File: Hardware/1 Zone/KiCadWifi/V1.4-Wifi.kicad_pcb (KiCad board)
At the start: 2 copper layers, 100 x 80 mm, 133 parts, among them CN11 Pinheader 1x12 P2.54 Horizont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, CN16 Pinheader 1x02 P2.54 Horizont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, J1 Screw_Terminal_01x02, Q1 IPD90N04S403ATMA1, Q10 PJA3404A, Q11 PJA3404A, Q12 BC816-16VL, Q8 UMH3NTN, SW1 K2-1102DP-G3SW-04, SW2 K2-1102DP-G3SW-04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

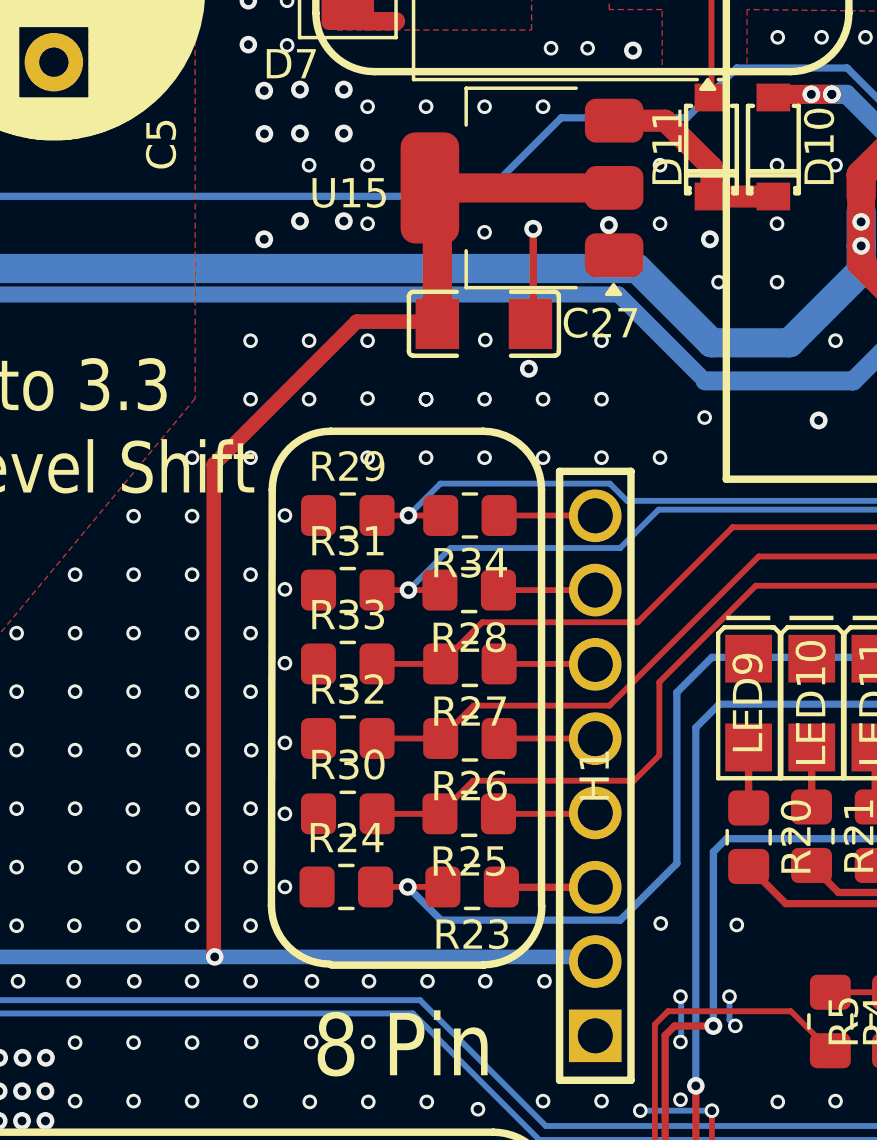
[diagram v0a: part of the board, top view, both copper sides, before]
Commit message: Changed C27 to T491B107M010AT due to availablility
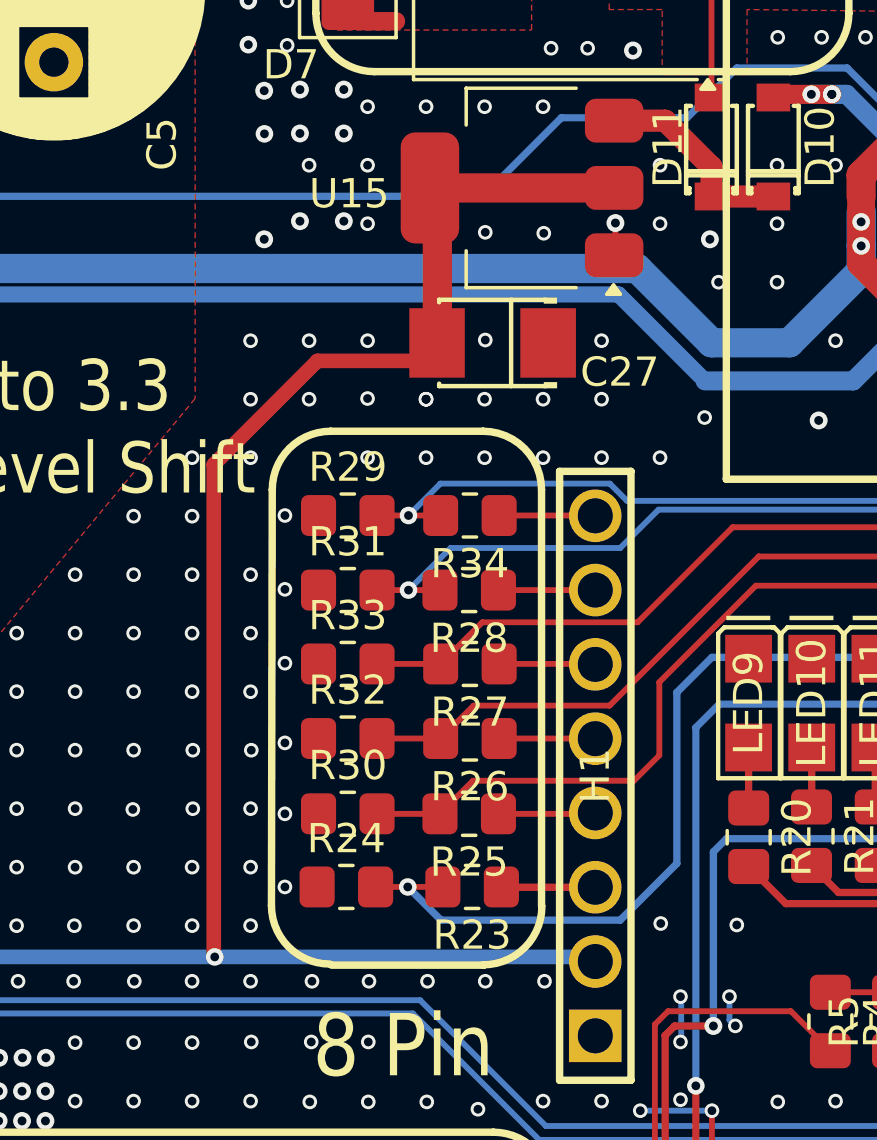
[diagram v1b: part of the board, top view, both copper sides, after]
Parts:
- C27: footprint V1.4-Wifi-easyedapro:C1206 -> V1.4-Wifi-easyedapro:CAP-SMD_L3.5-W2.8-R-RD
- moved C27 0.72 mm to (155.0, 98.2)
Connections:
- C27 pad 1: 3.3V -> GND
- C27 pad 2: GND -> 3.3V
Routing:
- net GND: track 66.4 -> 63.6 mm, vias 698 -> 697
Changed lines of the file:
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@@
 		)
 	)
-	(footprint "V1.4-Wifi-easyedapro:C1206"
+	(footprint "V1.4-Wifi-easyedapro:CAP-SMD_L3.5-W2.8-R-RD"
 		(layer "F.Cu")
-		(at 154.7035 97.5455)
+		(at 155 98.2)
 		(property "Reference" "C27"
-			(at 4.0035 0 0)
+			(at 4.35 1 0)
 			(layer "F.SilkS")
 			(effects
@@
 			)
 		)
-		(property "Datasheet" "https://atta.szlcsc.com/upload/public/pdf/source/20160103/1457707673200.pdf"
+		(property "Datasheet" "https://eu.mouser.com/datasheet/2/447/KEM_T2005_T491-3316937.pdf"
 			(at 0 0 0)
 			(layer "F.Fab")
@@
 			)
 		)
-		(property "Manufacturer" "SAMSUNG"
+		(property "Manufacturer" "KEMET"
 			(at 0 0 0)
 			(unlocked yes)
@@
 			)
 		)
-		(property "mpn" "CL31A107MQHNNNE"
+		(property "mpn" "T491B107M010AT"
 			(at 0 0 0)
 			(unlocked yes)
@@
 		(sheetfile "V1.4-Wifi.kicad_sch")
 		(fp_line
-			(start -2.5635 0.94)
-			(end -2.5635 -0.94)
+			(start -1.826 -1.476)
+			(end -1.826 -1.391)
 			(stroke
 				(width 0.1525)
@@
 		)
 		(fp_line
-			(start -2.411 -1.0925)
-			(end -0.926 -1.0925)
+			(start -1.826 -1.476)
+			(end 1.826 -1.476)
 			(stroke
 				(width 0.1525)
@@
 		)
 		(fp_line
-			(start -0.926 1.0925)
-			(end -2.411 1.0925)
+			(start -1.826 1.476)
+			(end -1.826 1.391)
 			(stroke
 				(width 0.1525)
@@
 		)
 		(fp_line
-			(start 0.926 1.0925)
-			(end 2.411 1.0925)
+			(start -1.826 1.476)
+			(end 1.826 1.476)
 			(stroke
 				(width 0.1525)
@@
 		)
 		(fp_line
-			(start 2.411 -1.0925)
-			(end 0.926 -1.0925)
+			(start 0.635 -1.476)
+			(end 0.635 1.476)
 			(stroke
 				(width 0.1525)
@@
 			(layer "F.SilkS")
 		)
-		(fp_line
-			(start 2.5635 0.94)
-			(end 2.5635 -0.94)
+		(fp_poly
+			(pts
+				(xy 1.75 -1.5525) (xy 1.75 -1.3405) (xy 2.207 -1.3405) (xy 2.207 -1.5525)
+			)
 			(stroke
-				(width 0.1525)
+				(width 0)
 				(type default)
 			)
+			(fill yes)
 			(layer "F.SilkS")
 		)
-		(fp_arc
-			(start -2.5635 -0.94)
-			(mid -2.518834 -1.047834)
-			(end -2.411 -1.0925)
+		(fp_poly
+			(pts
+				(xy 1.75 1.5525) (xy 1.75 1.3405) (xy 2.207 1.3405) (xy 2.207 1.5525)
+			)
 			(stroke
-				(width 0.1525)
+				(width 0)
 				(type default)
 			)
+			(fill yes)
 			(layer "F.SilkS")
 		)
-		(fp_arc
-			(start -2.411 1.0925)
-			(mid -2.518834 1.047834)
-			(end -2.5635 0.94)
+		(fp_poly
+			(pts
+				(xy -1.54 0.105) (xy -1.54 -0.105) (xy -0.7 -0.105) (xy -0.7 0.105)
+			)
 			(stroke
-				(width 0.1525)
+				(width 0)
 				(type default)
 			)
-			(layer "F.SilkS")
+			(fill yes)
+			(layer "Dwgs.User")
 		)
-		(fp_arc
-			(start 2.411 -1.0925)
-			(mid 2.518834 -1.047834)
-			(end 2.5635 -0.94)
+		(fp_poly
+			(pts
+				(xy 1.225 0.7) (xy 1.225 -0.7) (xy 1.015 -0.7) (xy 1.015 0.7)
+			)
 			(stroke
-				(width 0.1525)
+				(width 0)
 				(type default)
 			)
-			(layer "F.SilkS")
+			(fill yes)
+			(layer "Dwgs.User")
 		)
-		(fp_arc
-			(start 2.5635 0.94)
-			(mid 2.518834 1.047834)
-			(end 2.411 1.0925)
+		(fp_poly
+			(pts
+				(xy 1.54 0.105) (xy 1.54 -0.105) (xy 0.7 -0.105) (xy 0.7 0.105)
+			)
 			(stroke
-				(width 0.1525)
+				(width 0)
 				(type default)
 			)
-			(layer "F.SilkS")
+			(fill yes)
+			(layer "Dwgs.User")
 		)
 		(fp_poly
 			(pts
-				(xy -0.85 0.764) (xy -0.85 0.394) (xy -0.95 0.294) (xy -1.255 0.294) (xy -1.355 0.194) (xy -1.355 -0.194)
-				(xy -1.255 -0.294) (xy -0.95 -0.294) (xy -0.85 -0.394) (xy -0.85 -0.764) (xy -0.95 -0.864) (xy -2.235 -0.864)
-				(xy -2.335 -0.764) (xy -2.335 0.764) (xy -2.235 0.864) (xy -0.95 0.864)
+				(xy 1.75 -1.4) (xy 1.75 -0.7) (xy 1.33 -0.7) (xy 1.33 -1.4)
 			)
 			(stroke
@@
 			)
 			(fill yes)
-			(layer "F.Paste")
+			(layer "Dwgs.User")
 		)
 		(fp_poly
 			(pts
-				(xy 0.85 0.764) (xy 0.85 0.394) (xy 0.95 0.294) (xy 1.255 0.294) (xy 1.355 0.194) (xy 1.355 -0.194)
-				(xy 1.255 -0.294) (xy 0.95 -0.294) (xy 0.85 -0.394) (xy 0.85 -0.764) (xy 0.95 -0.864) (xy 2.235 -0.864)
-				(xy 2.335 -0.764) (xy 2.335 0.764) (xy 2.235 0.864) (xy 0.95 0.864)
+				(xy 1.75 1.4) (xy 1.75 0.7) (xy 1.33 0.7) (xy 1.33 1.4)
 			)
 			(stroke
@@
 			)
 			(fill yes)
-			(layer "F.Paste")
+			(layer "Dwgs.User")
 		)
 		(fp_poly
 			(pts
-				(xy -1.6 0.8) (xy -1.6 -0.8) (xy -1.1 -0.8) (xy -1.1 0.8)
+				(xy -1.75 1.1) (xy -1.75 -1.1) (xy -1.05 -1.1) (xy -1.05 1.1)
 			)
 			(stroke
@@
 		(fp_poly
 			(pts
-				(xy 1.6 0.8) (xy 1.6 -0.8) (xy 1.1 -0.8) (xy 1.1 0.8)
+				(xy 1.75 1.1) (xy 1.75 -1.1) (xy 1.05 -1.1) (xy 1.05 1.1)
 			)
 			(stroke
@@
 		)
 		(fp_line
-			(start -1.6 -0.8)
-			(end 1.6 -0.8)
+			(start -1.75 -1.4)
+			(end 1.75 -1.4)
 			(stroke
 				(width 0.051)
@@
 		)
 		(fp_line
-			(start -1.6 0.8)
-			(end -1.6 -0.8)
+			(start -1.75 1.4)
+			(end -1.75 -1.4)
 			(stroke
 				(width 0.051)
@@
 		)
 		(fp_line
-			(start 1.6 -0.8)
-			(end 1.6 0.8)
+			(start 1.75 -1.4)
+			(end 1.75 1.4)
 			(stroke
 				(width 0.051)
@@
 		)
 		(fp_line
-			(start 1.6 0.8)
-			(end -1.6 0.8)
+			(start 1.75 1.4)
+			(end -1.75 1.4)
 			(stroke
 				(width 0.051)
@@
 		(fp_poly
 			(pts
-				(xy -1.544567 0.777039) (xy -1.577039 0.744567) (xy -1.622961 0.744567) (xy -1.655433 0.777039)
-				(xy -1.655433 0.822961) (xy -1.622961 0.855433) (xy -1.577039 0.855433) (xy -1.544567 0.822961)
+				(xy 1.805433 -1.422961) (xy 1.772961 -1.455433) (xy 1.727039 -1.455433) (xy 1.694567 -1.422961)
+				(xy 1.694567 -1.377039) (xy 1.727039 -1.344567) (xy 1.772961 -1.344567) (xy 1.805433 -1.377039)
 			)
 			(stroke
@@
 		)
 		(pad "1" smd rect
-			(at -1.5925 0)
-			(size 1.485 1.728)
+			(at 1.8985 0)
+			(size 1.9 2.376)
 			(layers "F.Cu" "F.Mask" "F.Paste")
-			(net 36 "3.3V")
+			(net 1 "GND")
 			(pinfunction "1")
 			(pintype "input")
 		)
 		(pad "2" smd rect
-			(at 1.5925 0)
-			(size 1.485 1.728)
+			(at -1.8985 0)
+			(size 1.9 2.376)
 			(layers "F.Cu" "F.Mask" "F.Paste")
-			(net 1 "GND")
+			(net 36 "3.3V")
 			(pinfunction "2")
 			(pintype "input")
 		)
 		(embedded_fonts no)
-		(model "${KIPRJMOD}/EASYEDA_MODELS/C1206_L3.2-W1.6-H1.3.step"
+		(model "${KIPRJMOD}/EASYEDA_MODELS/CASE-B_L3.5-W2.8-H1.9.step"
 			(offset
 				(xyz 0 0 0)
@@
 			)
 			(rotate
-				(xyz -0 -0 -0)
+				(xyz -0 -0 -180)
 			)
 		)
@@
 	)
 	(segment
+		(start 159.2 95.157)
+		(end 159.157 95.2)
+		(width 0.2)
+		(layer "F.Cu")
+		(net 1)
+	)
+	(segment
 		(start 192.6775 74.0775)
 		(end 190.7 74.0775)
@@
 	)
 	(segment
-		(start 156.388 94.297)
-		(end 156.388 97.454)
-		(width 0.254)
-		(layer "F.Cu")
-		(net 1)
-	)
-	(segment
 		(start 172.4 108.75)
 		(end 171.645 108.75)
@@
 	)
 	(segment
-		(start 158.977 94.906)
-		(end 158.977 94.17)
-		(width 0.254)
-		(layer "F.Cu")
-		(net 1)
-	)
-	(segment
 		(start 190.65 85.7)
 		(end 190.0965 86.2535)
@@
 	)
 	(segment
+		(start 159.2 94.1)
+		(end 159.2 95.157)
+		(width 0.2)
+		(layer "F.Cu")
+		(net 1)
+	)
+	(segment
 		(start 196.9 78.95)
 		(end 196.55 78.6)
@@
 	)
 	(via
-		(at 156.388 94.297)
-		(size 0.61)
-		(drill 0.305)
-		(layers "F.Cu" "B.Cu")
-		(net 1)
-	)
-	(via
 		(at 192.911 84.496)
 		(size 0.61)
@@
 	)
 	(via
-		(at 158.977 94.17)
+		(at 159.2 94.1)
 		(size 0.61)
 		(drill 0.305)
@@
 	)
 	(via
-		(at 154.726 94.417)
+		(at 154.75 94.417)
 		(size 0.5)
 		(drill 0.3)
@@
 	)
 	(via
+		(at 156.75 94.45)
+		(size 0.5)
+		(drill 0.3)
+		(layers "F.Cu" "B.Cu")
+		(net 1)
+	)
+	(via
 		(at 174.726 94.123)
 		(size 0.5)
@@
 	)
 	(via
-		(at 156.2405 99.083)
-		(size 0.61)
-		(drill 0.304)
-		(layers "F.Cu" "B.Cu")
-		(net 1)
-	)
-	(via
 		(at 174.726 78.123)
 		(size 0.5)
@@
 	(segment
 		(start 145.466 102.359)
-		(end 150.353 97.472)
+		(end 149.0125 98.8125)
 		(width 0.5)
 		(layer "F.Cu")
@@
 	)
 	(segment
-		(start 106.05 119)
-		(end 106.05 119.7)
+		(start 152.489 98.8125)
+		(end 153.1015 98.2)
 		(width 0.5)
 		(layer "F.Cu")
@@
 	)
 	(segment
-		(start 106.05 128.9)
-		(end 106.05 129.6)
+		(start 106.05 119)
+		(end 106.05 119.7)
 		(width 0.5)
 		(layer "F.Cu")
@@
 	)
 	(segment
-		(start 150.353 97.472)
-		(end 153.0375 97.472)
+		(start 106.05 128.9)
+		(end 106.05 129.6)
 		(width 0.5)
 		(layer "F.Cu")
@@
 	)
 	(segment
-		(start 153.111 97.5455)
-		(end 153.111 92.974)
+		(start 153.1015 98.2)
+		(end 153.111 98.1905)
 		(width 1)
 		(layer "F.Cu")
@@
 	)
 	(segment
-		(start 145.466 119.1585)
-		(end 145.5 119.1925)
+		(start 149.0125 98.8125)
+		(end 152.489 98.8125)
 		(width 0.5)
 		(layer "F.Cu")
@@
 	)
 	(segment
-		(start 145.466 102.359)
-		(end 145.466 119.1585)
+		(start 145.466 119.1585)
+		(end 145.466 102.359)
 		(width 0.5)
 		(layer "F.Cu")
@@
 	)
 	(segment
+		(start 145.5 119.1925)
+		(end 145.466 119.1585)
+		(width 0.5)
+		(layer "F.Cu")
+		(net 36)
+	)
+	(segment
 		(start 106.05 122.5)
 		(end 106.05 128.9)
@@
 		(layer "F.Cu")
 		(net 36)
+	)
+	(segment
+		(start 153.111 98.1905)
+		(end 153.111 92.974)
+		(width 1)
+		(layer "F.Cu")
+		(net 36)

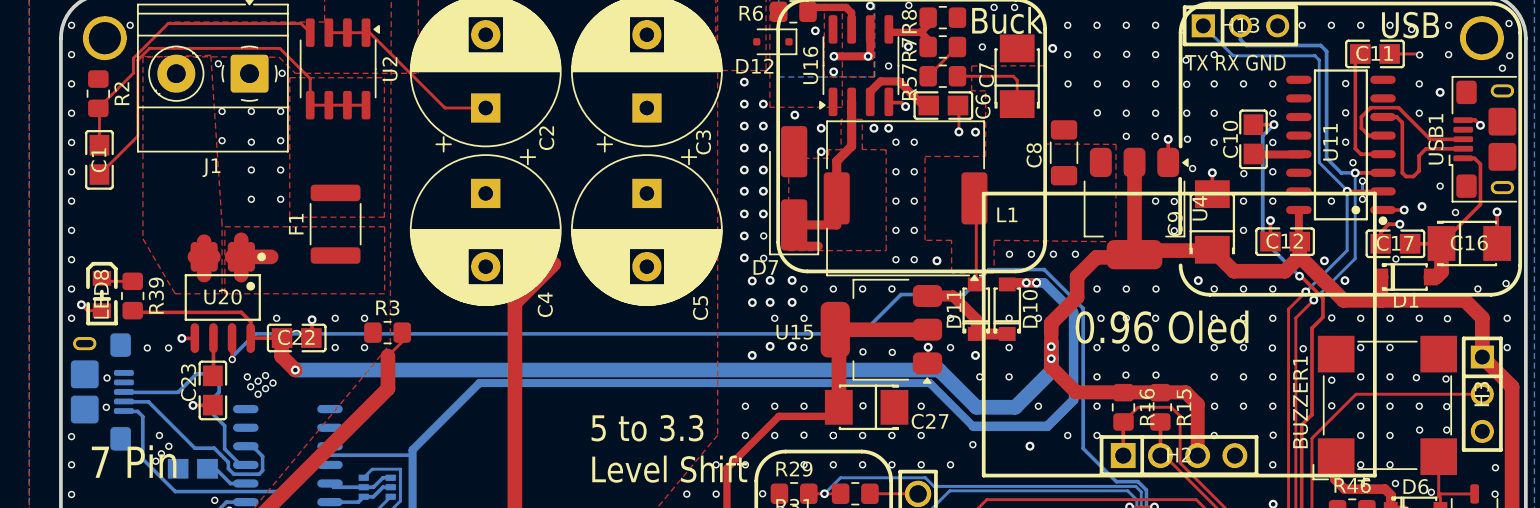
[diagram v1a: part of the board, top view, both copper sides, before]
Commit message: Moved C27 to avoid disrupting D+_E, D-_E return paths
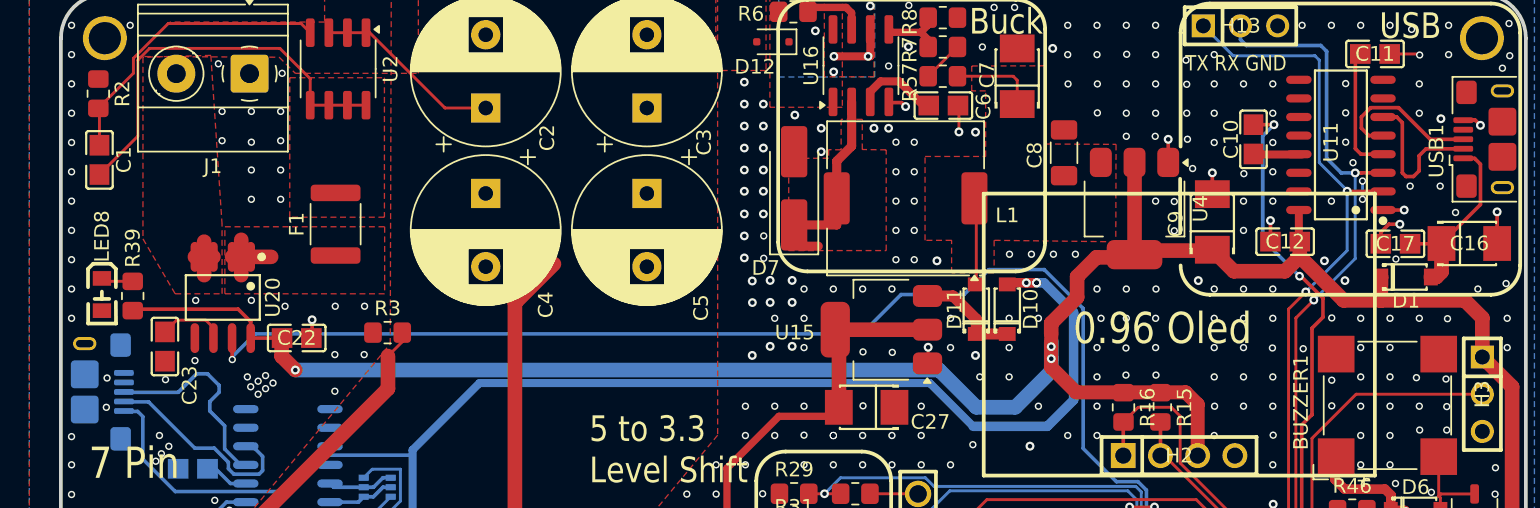
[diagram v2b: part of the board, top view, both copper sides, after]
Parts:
- moved C23 4.44 mm to (107.1, 94.0)
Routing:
- net GND: track 63.6 -> 59.8 mm
- net Net-(U20-FILTER): track 2.50 -> 4.56 mm
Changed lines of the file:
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@@
 		(at 102.8 90.5 -90)
 		(property "Reference" "LED8"
-			(at 0 0 90)
+			(at -3.97 -0.005 90)
 			(layer "F.SilkS")
 			(effects
@@
 		(at 111.049 90.701 180)
 		(property "Reference" "U20"
-			(at 0 0 180)
+			(at -3.421 0 270)
 			(layer "F.SilkS")
 			(effects
@@
 		(at 102.63 81.31 90)
 		(property "Reference" "C1"
-			(at 0 0 90)
+			(at 0.01 1.67 90)
 			(layer "F.SilkS")
 			(effects
@@
 		(tags "resistor handsolder")
 		(property "Reference" "R39"
-			(at 0 -1.65 90)
+			(at -3.28 -0.01 90)
 			(layer "F.SilkS")
 			(effects
@@
 		(tags "USB Micro-B horizontal SMD")
 		(property "Reference" "USB1"
-			(at 0 -4.5 90)
+			(at -0.8 -4.5 90)
 			(layer "F.SilkS")
 			(effects
@@
 	(footprint "V1.4-Wifi-easyedapro:C0805"
 		(layer "F.Cu")
-		(at 110.3735 97.049 -90)
+		(at 107.1 94.05 -90)
 		(property "Reference" "C23"
-			(at -0.549 1.6235 270)
+			(at 2.65 -1.69 270)
 			(layer "F.SilkS")
 			(effects
@@
 		(at 115.494 102.766 90)
 		(property "Reference" "U22"
-			(at 0 0 270)
+			(at -6.034 0 0)
 			(layer "B.SilkS")
 			(effects
@@
 		(tags "USB Micro-B horizontal SMD")
 		(property "Reference" "USB2"
-			(at 0 4.5 270)
+			(at -0.05 4.675 270)
 			(layer "B.SilkS")
 			(effects
@@
 	)
 	(segment
-		(start 102.8 91.6)
-		(end 101.8 91.6)
-		(width 0.2)
-		(layer "F.Cu")
-		(net 1)
-	)
-	(segment
 		(start 191.694 84.732)
 		(end 190.2485 84.732)
@@
 	)
 	(segment
-		(start 110.3615 98.067)
-		(end 109.017 98.067)
-		(width 0.25)
-		(layer "F.Cu")
-		(net 1)
-	)
-	(segment
 		(start 182.566 86.891)
 		(end 182.566 85.45)
@@
 	)
 	(segment
-		(start 101.8 91.6)
-		(end 101.4 91.2)
-		(width 0.2)
-		(layer "F.Cu")
-		(net 1)
-	)
-	(segment
 		(start 196.49 78.606)
 		(end 195.731 78.606)
@@
 	)
 	(segment
-		(start 109.1225 93.495)
-		(end 108.255 93.495)
-		(width 0.25)
-		(layer "F.Cu")
-		(net 1)
-	)
-	(segment
 		(start 198.0375 87.018)
 		(end 198.0375 84.859)
@@
 	)
 	(via
-		(at 108.255 93.495)
-		(size 0.61)
-		(drill 0.305)
-		(layers "F.Cu" "B.Cu")
-		(net 1)
-	)
-	(via
 		(at 105.3 131.935)
 		(size 0.5)
@@
 	)
 	(via
-		(at 109.017 98.067)
-		(size 0.61)
-		(drill 0.305)
-		(layers "F.Cu" "B.Cu")
-		(net 1)
-	)
-	(via
 		(at 172.6 126.1)
 		(size 0.5)
@@
 	)
 	(via
-		(at 192.911 84.496)
-		(size 0.61)
-		(drill 0.304)
-		(layers "F.Cu" "B.Cu")
-		(net 1)
-	)
-	(via
 		(at 174.75 96)
 		(size 0.5)
@@
 	)
 	(via
-		(at 101.4 91.2)
-		(size 0.61)
-		(drill 0.305)
-		(layers "F.Cu" "B.Cu")
-		(net 1)
-	)
-	(via
 		(at 136.725 118.1)
 		(size 0.5)
@@
 	)
 	(via
-		(at 120.726 94.123)
+		(at 120.7 94.6)
 		(size 0.5)
 		(drill 0.3)
@@
 	)
 	(via
+		(at 192.1 83.1)
+		(size 0.5)
+		(drill 0.3)
+		(layers "F.Cu" "B.Cu")
+		(net 1)
+	)
+	(via
 		(at 163.1 120.55)
 		(size 0.5)
@@
 	)
 	(via
-		(at 105.9 94.15)
+		(at 107.14 96.31)
 		(size 0.5)
 		(drill 0.3)
@@
 	)
 	(via
-		(at 107.35 94.15)
+		(at 109.15 95.01)
 		(size 0.5)
 		(drill 0.3)
@@
 	)
 	(via
-		(at 114.726 92.123)
+		(at 115.3 91.3)
 		(size 0.5)
 		(drill 0.3)
@@
 	)
 	(via
+		(at 109.2 90.9)
+		(size 0.5)
+		(drill 0.3)
+		(layers "F.Cu" "B.Cu")
+		(net 1)
+	)
+	(via
 		(at 187.173 141.56)
 		(size 0.61)
@@
 	)
 	(via
-		(at 118.726 92.123)
+		(at 118.726 91.3)
 		(size 0.5)
 		(drill 0.3)
@@
 	)
 	(via
-		(at 120.726 92.123)
+		(at 120.726 91.3)
 		(size 0.5)
 		(drill 0.3)
@@
 	)
 	(via
-		(at 118.726 94.123)
+		(at 118.7 94.6)
 		(size 0.5)
 		(drill 0.3)
@@
 	)
 	(via
-		(at 194.15 76.7)
+		(at 194.2 78.5)
 		(size 0.61)
 		(drill 0.304)
@@
 	)
 	(via
+		(at 113 90.9)
+		(size 0.5)
+		(drill 0.3)
+		(layers "F.Cu" "B.Cu")
+		(net 1)
+	)
+	(via
 		(at 138.726 112.123)
 		(size 0.5)
@@
 	)
 	(via
+		(at 118.7 97.1)
+		(size 0.5)
+		(drill 0.3)
+		(layers "F.Cu" "B.Cu")
+		(net 1)
+	)
+	(via
 		(at 160.706 138.58)
 		(size 0.61)
@@
 	)
 	(segment
-		(start 105.017 91.717)
-		(end 112.319 91.717)
-		(width 0.25)
-		(layer "F.Cu")
-		(net 2)
-	)
-	(segment
 		(start 173.286 81.76)
 		(end 173.286 87.5)
@@
 	)
 	(segment
+		(start 105.017 91.717)
+		(end 105.234 91.5)
+		(width 0.25)
+		(layer "F.Cu")
+		(net 2)
+	)
+	(segment
 		(start 177.5035 121.5955)
 		(end 176.2455 122.8535)
@@
 	)
 	(segment
+		(start 105.234 91.5)
+		(end 112.102 91.5)
+		(width 0.25)
+		(layer "F.Cu")
+		(net 2)
+	)
+	(segment
 		(start 184.5035 84.732)
 		(end 184.5035 86.8285)
@@
 	)
 	(segment
-		(start 112.319 91.717)
-		(end 112.954 92.352)
-		(width 0.25)
-		(layer "F.Cu")
-		(net 2)
-	)
-	(segment
 		(start 196.587 136.96)
 		(end 194.5 136.96)
@@
 	)
 	(segment
-		(start 112.954 92.352)
-		(end 112.954 93.4735)
-		(width 0.25)
-		(layer "F.Cu")
-		(net 2)
-	)
-	(segment
 		(start 190.1 89.3325)
 		(end 190.1285 89.304)
@@
 	)
 	(segment
+		(start 112.102 91.5)
+		(end 112.954 92.352)
+		(width 0.25)
+		(layer "F.Cu")
+		(net 2)
+	)
+	(segment
 		(start 167.601 93.1875)
 		(end 167.601 94.0605)
@@
 	)
 	(segment
+		(start 112.954 92.352)
+		(end 112.954 93.4735)
+		(width 0.25)
+		(layer "F.Cu")
+		(net 2)
+	)
+	(segment
 		(start 186.9145 145.691)
 		(end 189.455 145.691)
@@
 	)
 	(segment
+		(start 107.9 92.25)
+		(end 107.1 93.05)
+		(width 0.2)
+		(layer "F.Cu")
+		(net 68)
+	)
+	(segment
+		(start 109.89 92.25)
+		(end 107.9 92.25)
+		(width 0.2)
+		(layer "F.Cu")
+		(net 68)
+	)
+	(segment
 		(start 110.414 93.4735)
-		(end 110.414 95.9785)
-		(width 0.25)
+		(end 110.414 92.774)
+		(width 0.2)
+		(layer "F.Cu")
+		(net 68)
+	)
+	(segment
+		(start 110.414 92.774)
+		(end 109.89 92.25)
+		(width 0.2)
 		(layer "F.Cu")
 		(net 68)
